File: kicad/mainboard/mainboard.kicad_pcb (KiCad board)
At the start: 2 copper layers, 40 x 57 mm, 29 parts, among them J1 USB_C_Receptacle_USB2.0_16P, J2 Conn_01x03_Socket, J3 Conn_01x06_Socket, J4 Conn_01x06_Socket, U1 TPD1E05U06DYA, U2 TPD1E05U06DYA, U3 ESP32-S3-WROOM-1, U4 TPD1E05U06DYA, U5 TLV1117-33

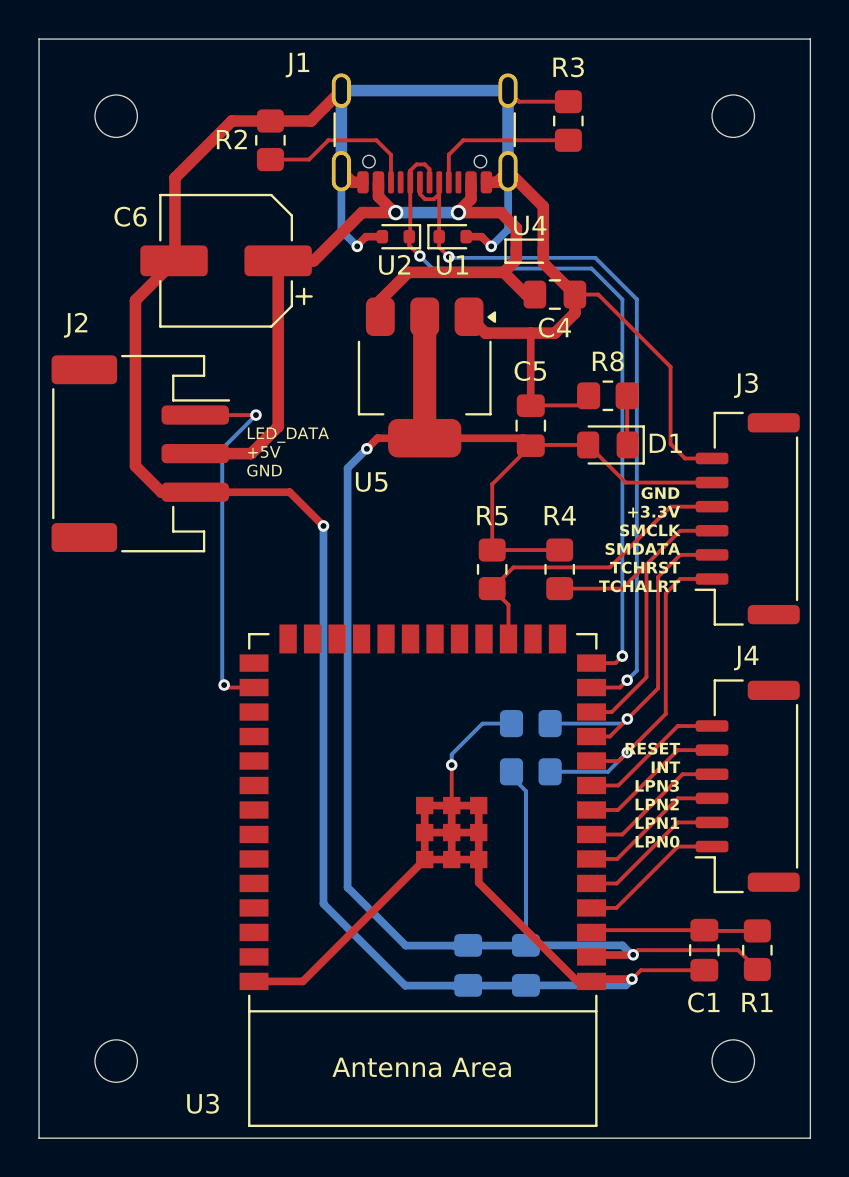
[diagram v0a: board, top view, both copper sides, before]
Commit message: re-route mainboard for better connectors
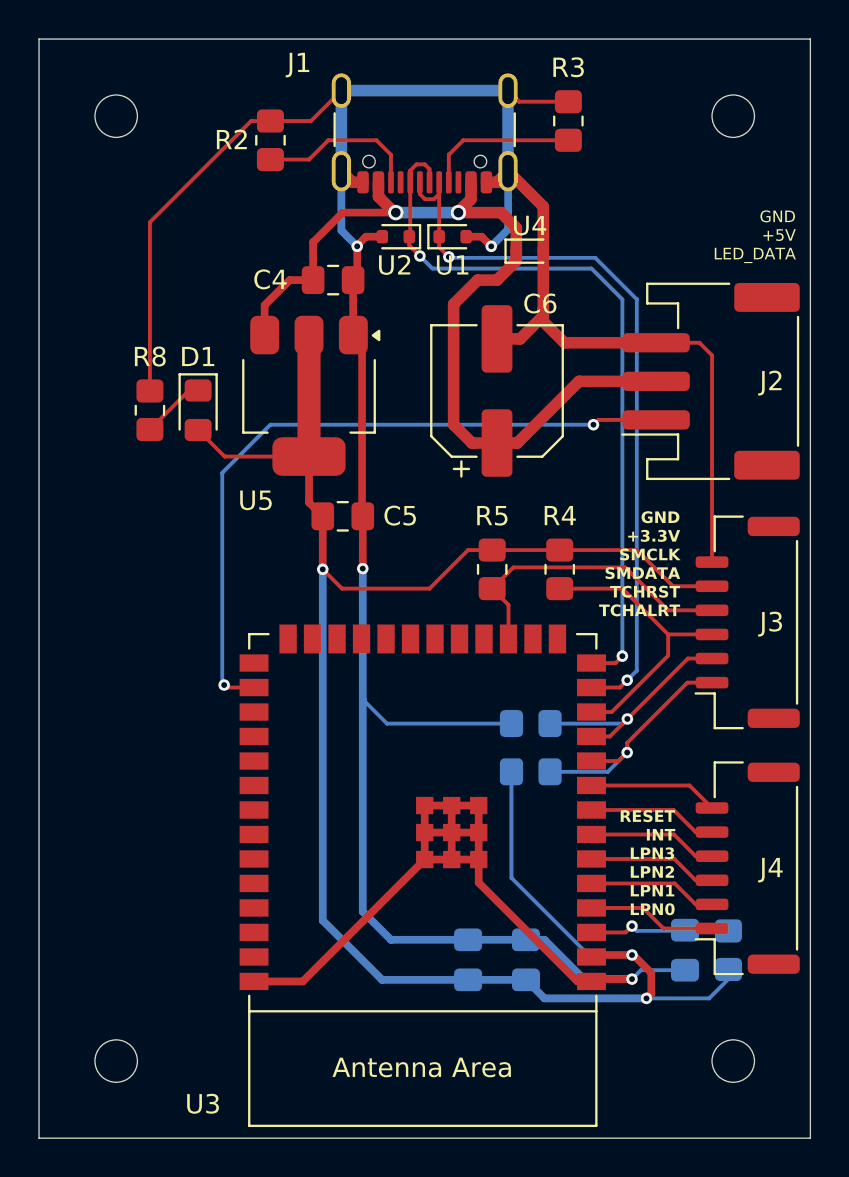
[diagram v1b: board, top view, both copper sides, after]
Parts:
- C1, R1: moved to B.Cu
- moved G*** 44.1 mm to (109.2, 108.0)
- moved J2 29.8 mm to (139.1, 82.0), turned to 90 degrees
- moved R8 23.8 mm to (110.0, 83.5), turned to 90 degrees
- moved D1 21.3 mm to (112.5, 83.5), turned to -90 degrees
- moved C6 15.6 mm to (128.0, 82.5), turned to 90 degrees
- moved C4 11.5 mm to (119.5, 76.8)
- moved C5 10.8 mm to (120.0, 89.0), turned to 0 degrees
- moved U5 6.07 mm to (118.2, 82.8)
- moved J3 5.38 mm to (141.0, 94.5)
- moved J4 4.25 mm to (141.0, 107.2)
- moved R1 1.50 mm to (140.0, 111.5)
- moved C1 1.00 mm to (137.8, 111.5)
- moved C2 0.29 mm to (129.5, 112.0), turned to -90 degrees
- moved C3 0.29 mm to (126.5, 112.0), turned to -90 degrees
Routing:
- net LED_DATA: track 19.5 -> 36.3 mm
- net +3.3V: track 93.4 -> 101.1 mm, vias 2 -> 3
- net TOUCH_RESET: track 17.6 -> 12.0 mm
- net TOUCH_ALERT: track 18.2 -> 12.6 mm
- net GND: track 194.4 -> 189.1 mm, vias 5 -> 4
- net SMDATA: track 18.6 -> 15.2 mm
- net +5V: track 43.5 -> 46.2 mm
- net Net-(U3-EN): track 8.66 -> 7.34 mm, vias 0 -> 1
- net TOF_LPN0: track 7.57 -> 6.69 mm
- net TOF_LPN1: track 7.56 -> 6.70 mm
- net TOF_LPN2: track 7.55 -> 6.71 mm
- net TOF_LPN3: track 7.54 -> 6.72 mm
- net TOF_INT: track 7.54 -> 6.72 mm
- net TOF_RESET: track 7.53 -> 6.73 mm
- net Net-(D1-K): track 2.56 -> 3.34 mm
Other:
- board text added: "GND +5V LED_DATA"
- board text removed: "LED_DATA +5V GND"

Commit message: change led to 11
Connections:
- U3 pad 19: unconnected-(U3-GPIO11/TOUCH11/ADC2_CH0/FSPID/FSPIIO5/SUBSPID-Pad19) -> LED_DATA
- U3 pad 28: LED_DATA -> unconnected-(U3-SPIIO6/GPIO35/FSPID/SUBSPID-Pad28)
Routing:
- net LED_DATA: track 36.3 -> 18.2 mm, vias 2 -> 0
- net +3.3V: track 101.1 -> 101.8 mm, vias 3 -> 4
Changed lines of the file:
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@@
 	(net 36 "unconnected-(U3-GPIO1{slash}TOUCH1{slash}ADC1_CH0-Pad39)")
 	(net 37 "unconnected-(U3-GPIO14{slash}TOUCH14{slash}ADC2_CH3{slash}FSPIWP{slash}FSPIDQS{slash}SUBSPIWP-Pad22)")
-	(net 38 "unconnected-(U3-GPIO11{slash}TOUCH11{slash}ADC2_CH0{slash}FSPID{slash}FSPIIO5{slash}SUBSPID-Pad19)")
+	(net 38 "unconnected-(U3-SPIIO6{slash}GPIO35{slash}FSPID{slash}SUBSPID-Pad28)")
 	(net 39 "unconnected-(U3-GPIO12{slash}TOUCH12{slash}ADC2_CH1{slash}FSPICLK{slash}FSPIIO6{slash}SUBSPICLK-Pad20)")
 	(net 40 "unconnected-(U3-MTMS{slash}GPIO42-Pad35)")
@@
 			(size 1.5 0.9)
 			(layers "F.Cu" "F.Mask" "F.Paste")
-			(net 38 "unconnected-(U3-GPIO11{slash}TOUCH11{slash}ADC2_CH0{slash}FSPID{slash}FSPIIO5{slash}SUBSPID-Pad19)")
+			(net 34 "LED_DATA")
 			(pinfunction "GPIO11/TOUCH11/ADC2_CH0/FSPID/FSPIIO5/SUBSPID")
-			(pintype "bidirectional+no_connect")
+			(pintype "bidirectional")
 		)
 		(pad "20" smd rect
@@
 			(size 1.5 0.9)
 			(layers "F.Cu" "F.Mask" "F.Paste")
-			(net 34 "LED_DATA")
+			(net 38 "unconnected-(U3-SPIIO6{slash}GPIO35{slash}FSPID{slash}SUBSPID-Pad28)")
 			(pinfunction "SPIIO6/GPIO35/FSPID/SUBSPID")
-			(pintype "bidirectional")
+			(pintype "bidirectional+no_connect")
 		)
 		(pad "29" smd rect
@@
 	)
 	(segment
-		(start 127.05 108)
-		(end 132.17 113.12)
+		(start 121.0375 92.75)
+		(end 121.0375 89)
 		(width 0.4)
 		(layer "F.Cu")
@@
 	)
 	(segment
-		(start 121.0375 91.7125)
-		(end 121.0375 89)
+		(start 127.05 108)
+		(end 132.17 113.12)
 		(width 0.4)
 		(layer "F.Cu")
@@
 	)
 	(via
-		(at 121.0375 91.7125)
+		(at 121.0375 92.75)
 		(size 0.6)
 		(drill 0.3)
@@
 	)
 	(segment
+		(start 121.0375 92.75)
+		(end 121.0375 98.5)
+		(width 0.4)
+		(layer "B.Cu")
+		(net 1)
+	)
+	(segment
 		(start 128.57 66.925)
 		(end 128.57 71.105)
@@
 	)
 	(segment
-		(start 121.0375 91.7125)
-		(end 121.0375 98.5)
-		(width 0.4)
-		(layer "B.Cu")
-		(net 1)
-	)
-	(segment
 		(start 128.75 99.75)
 		(end 122.2875 99.75)
@@
 	)
 	(segment
-		(start 127.75 90.75)
+		(start 129.5 90.75)
 		(end 131.25 90.75)
 		(width 0.2)
@@
 	)
 	(segment
-		(start 119.9625 92.75)
-		(end 118.9625 91.75)
+		(start 127.75 90.75)
+		(end 129.5 90.75)
 		(width 0.2)
 		(layer "F.Cu")
@@
 	)
 	(segment
-		(start 118.25 88.2875)
+		(start 118.9625 91.25)
 		(end 118.9625 89)
 		(width 0.4)
@@
 	)
 	(segment
-		(start 118.9625 91.75)
+		(start 118.25 88.2875)
 		(end 118.9625 89)
 		(width 0.4)
@@
 	)
 	(segment
-		(start 126.5 90.75)
-		(end 127.75 90.75)
-		(width 0.2)
-		(layer "F.Cu")
-		(net 3)
-	)
-	(segment
 		(start 136 113.75)
 		(end 136 112.679176)
@@
 		(net 3)
 	)
-	(segment
-		(start 124.5 92.75)
-		(end 126.5 90.75)
-		(width 0.2)
-		(layer "F.Cu")
-		(net 3)
-	)
-	(segment
-		(start 119.9625 92.75)
-		(end 124.5 92.75)
-		(width 0.2)
-		(layer "F.Cu")
+	(via
+		(at 129.5 90.75)
+		(size 0.6)
+		(drill 0.3)
+		(layers "F.Cu" "B.Cu")
 		(net 3)
 	)
@@
 	)
 	(via
-		(at 118.9625 91.75)
+		(at 118.9625 91.25)
 		(size 0.6)
 		(drill 0.3)
@@
 	)
 	(segment
-		(start 118.9625 91.75)
-		(end 118.9625 109.9625)
+		(start 118.9625 109.9625)
+		(end 122.0375 113.0375)
 		(width 0.4)
 		(layer "B.Cu")
@@
 	)
 	(segment
+		(start 129.5 90.75)
+		(end 129 91.25)
+		(width 0.2)
+		(layer "B.Cu")
+		(net 3)
+	)
+	(segment
 		(start 132.75 111.75)
 		(end 135 111.75)
@@
 	)
 	(segment
-		(start 122.0375 113.0375)
-		(end 129.5 113.0375)
-		(width 0.4)
-		(layer "B.Cu")
-		(net 3)
-	)
-	(segment
 		(start 128.75 107.75)
 		(end 132.75 111.75)
@@
 	)
 	(segment
-		(start 118.9625 109.9625)
-		(end 122.0375 113.0375)
+		(start 122.0375 113.0375)
+		(end 129.5 113.0375)
+		(width 0.4)
+		(layer "B.Cu")
+		(net 3)
+	)
+	(segment
+		(start 118.9625 91.25)
+		(end 118.9625 109.9625)
 		(width 0.4)
 		(layer "B.Cu")
@@
 	)
 	(segment
+		(start 129 91.25)
+		(end 118.9625 91.25)
+		(width 0.2)
+		(layer "B.Cu")
+		(net 3)
+	)
+	(segment
 		(start 135.75 114)
 		(end 139 114)
@@
 	)
 	(segment
-		(start 113.85 97.75)
-		(end 113.98 97.88)
+		(start 128.75 88.5)
+		(end 127.25 88.5)
 		(width 0.2)
 		(layer "F.Cu")
@@
 	)
 	(segment
-		(start 113.98 97.88)
-		(end 115.4 97.88)
+		(start 127.25 88.5)
+		(end 126.055 89.695)
 		(width 0.2)
 		(layer "F.Cu")
@@
 	(segment
 		(start 133.25 84)
-		(end 133 84.25)
+		(end 128.75 88.5)
 		(width 0.2)
 		(layer "F.Cu")
 		(net 34)
 	)
-	(via
-		(at 113.85 97.75)
-		(size 0.6)
-		(drill 0.3)
-		(layers "F.Cu" "B.Cu")
-		(net 34)
-	)
-	(via
-		(at 133 84.25)
-		(size 0.6)
-		(drill 0.3)
-		(layers "F.Cu" "B.Cu")
-		(net 34)
-	)
-	(segment
-		(start 116.25 84.25)
-		(end 133 84.25)
-		(width 0.2)
-		(layer "B.Cu")
-		(net 34)
-	)
 	(segment
-		(start 113.85 97.75)
-		(end 113.75 97.65)
+		(start 126.055 89.695)
+		(end 126.055 95.36)
 		(width 0.2)
-		(layer "B.Cu")
-		(net 34)
-	)
-	(segment
-		(start 113.75 97.65)
-		(end 113.75 86.75)
-		(width 0.2)
-		(layer "B.Cu")
-		(net 34)
-	)
-	(segment
-		(start 113.75 86.75)
-		(end 116.25 84.25)
-		(width 0.2)
-		(layer "B.Cu")
+		(layer "F.Cu")
 		(net 34)
 	)

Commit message: final tweaks
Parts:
- moved G*** 2.02 mm to (109.5, 110.0)
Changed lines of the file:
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@@
 	(footprint "Logo:Snep_Copper"
 		(layer "F.Cu")
-		(at 109.25 108)
+		(at 109.5 110)
 		(property "Reference" "G***"
 			(at 0 0 0)

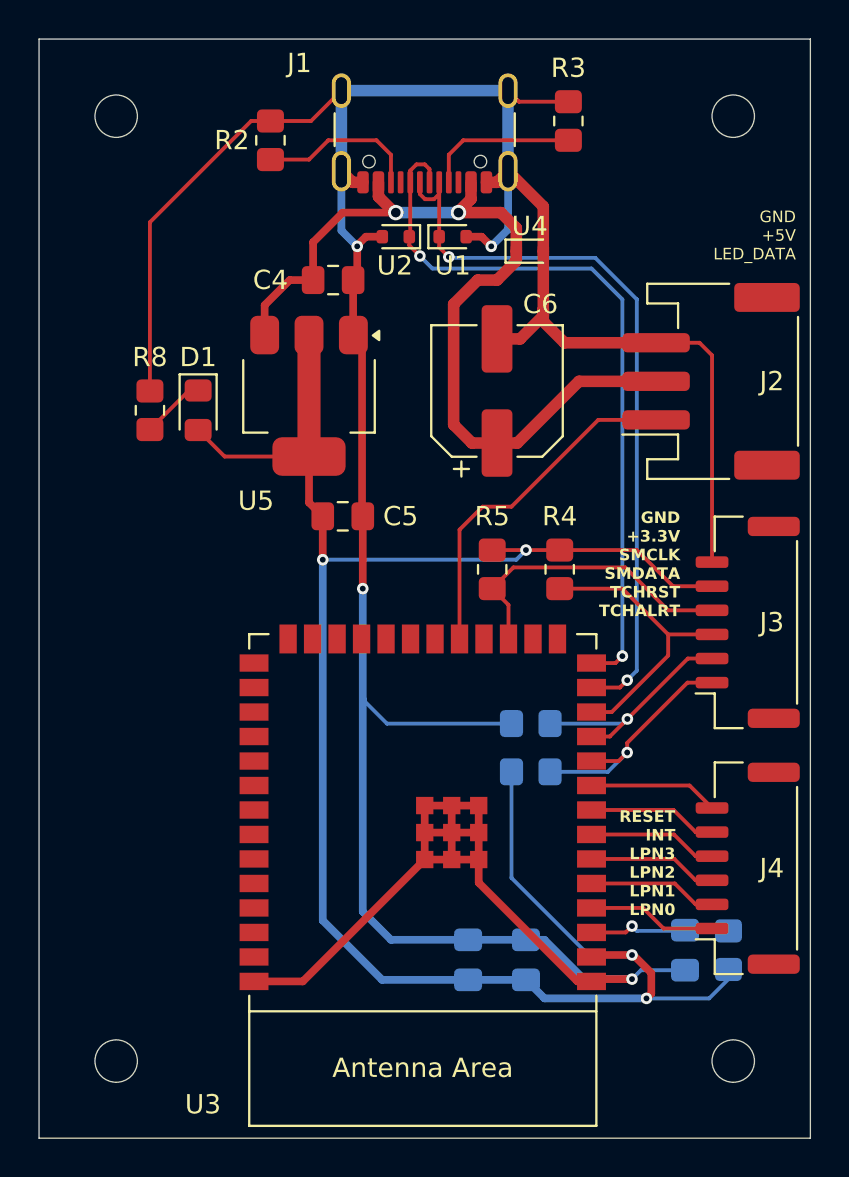
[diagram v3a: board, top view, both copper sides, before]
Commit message: route LDO after TVS
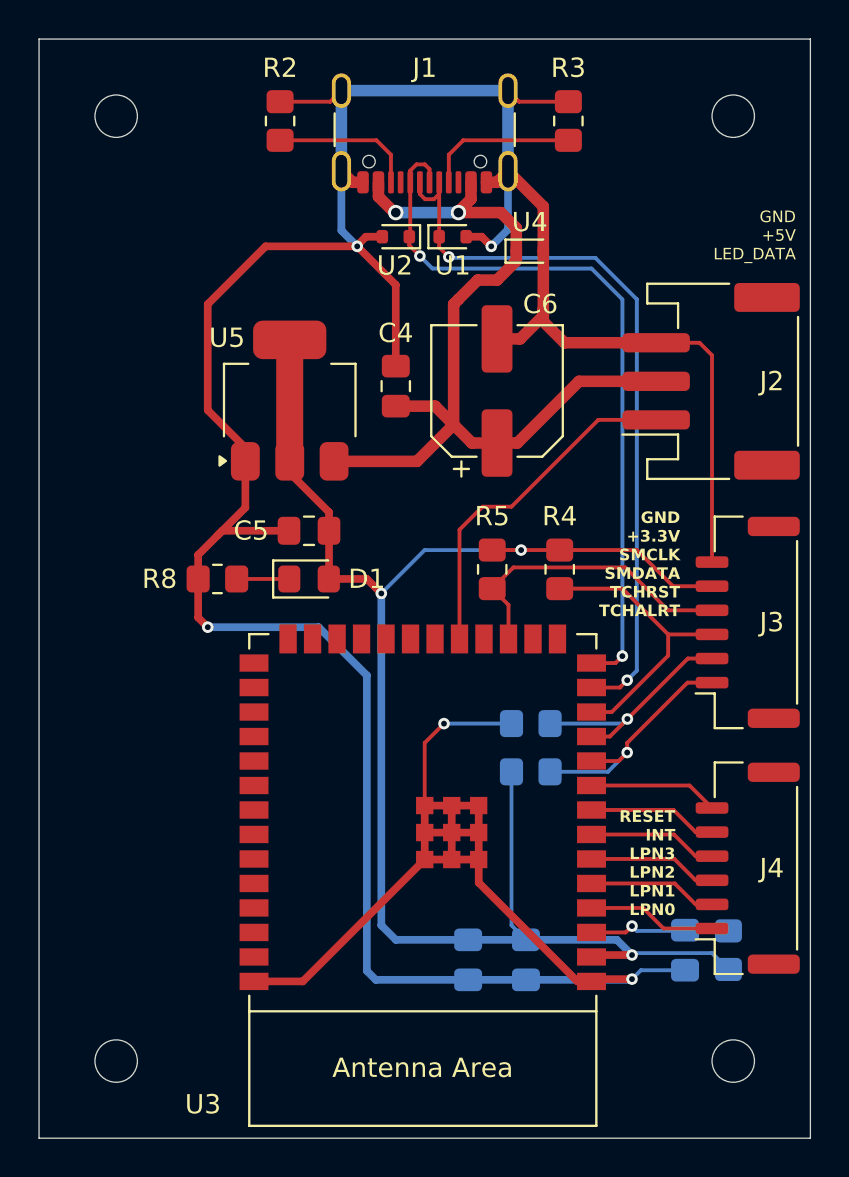
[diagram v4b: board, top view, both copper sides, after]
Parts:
- moved D1 10.5 mm to (118.2, 92.2), turned to 0 degrees
- moved R8 9.42 mm to (113.5, 92.2), turned to 180 degrees
- moved C4 6.39 mm to (122.8, 82.2), turned to 90 degrees
- moved C5 1.90 mm to (118.2, 89.8), turned to 180 degrees
- moved R2 1.12 mm to (116.8, 68.5)
- moved U5 1.03 mm to (117.2, 83.0), turned to 90 degrees
- turned C2 to 90 degrees
- turned C3 to 90 degrees
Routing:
- net +3.3V: track 101.8 -> 84.6 mm, vias 4 -> 3
- net GND: track 189.1 -> 197.9 mm, vias 4 -> 5
- net +5V: track 46.2 -> 45.1 mm
- net Net-(J1-CC2): track 8.40 -> 7.49 mm
- net Net-(D1-K): track 3.34 -> 2.72 mm

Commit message: gerber and bom
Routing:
- net +3.3V: track 84.6 -> 84.1 mm
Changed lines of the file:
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@@
-	)
-	(segment
-		(start 129.25 90.75)
-		(end 129.5 90.75)
-		(width 0.2)
-		(layer "F.Cu")
-		(net 3)
 	)
 	(segment
@@
 	)
 	(segment
-		(start 129.5 90.75)
+		(start 129.25 90.75)
 		(end 131.25 90.75)
 		(width 0.2)
@@
 	)
 	(segment
-		(start 140 113)
-		(end 140 112.5)
-		(width 0.2)
-		(layer "B.Cu")
-		(net 3)
-	)
-	(segment
 		(start 134.2125 110.9625)
 		(end 135 111.75)
@@
 	)
 	(segment
-		(start 127 76.75)
-		(end 126 77.75)
-		(width 0.6)
-		(layer "F.Cu")
-		(net 4)
-	)
-	(segment
 		(start 129 74.05)
 		(end 129 75.25)
@@
 	)
 	(segment
-		(start 126 77.75)
-		(end 125.75 78)
-		(width 0.6)
-		(layer "F.Cu")
+		(start 125.75 78)
+		(end 127 76.75)
+		(width 0.6)
+		(layer "F.Cu")

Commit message: changes
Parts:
- moved R8 4.56 mm to (118.0, 91.5), turned to 90 degrees
- moved G*** 4.50 mm to (109.5, 105.5)
- moved D1 3.09 mm to (115.2, 91.5), turned to 90 degrees
- moved C5 2.83 mm to (116.2, 87.8), turned to 0 degrees
- moved U5 1.35 mm to (116.0, 82.5), turned to 180 degrees
- moved C4 1.03 mm to (122.5, 81.2), turned to -90 degrees
- turned C2 to -90 degrees
- turned C3 to -90 degrees
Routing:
- net +3.3V: track 84.1 -> 111.7 mm
- net GND: track 197.9 -> 183.5 mm, vias 5 -> 4
- net +5V: track 45.1 -> 42.3 mm
